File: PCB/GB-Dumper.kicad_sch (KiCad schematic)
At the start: 12 parts, among them J1 GameBoy_Cartridge_MountingPin, J2 Conn_01x03_Male, J3 Conn_01x02_Male, J4 Conn_01x04_Female, U1 74HC595, U2 74HC595

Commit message: -update design to 0.7 (clk 6 rst jumpers)
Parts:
- added C1: 22 µF, Capacitor_THT:CP_Radial_D4.0mm_P2.00mm, symbol Device:C_Polarized_Small
- R1, R2, R3, R4: value 470 -> 470Ω
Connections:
- net GND: now also C1.2
- net at A1.27 (+5V), J3.1 (Pin_1), J4.2 (Pin_2)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: now also C1.1
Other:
- moved on the sheet: R4
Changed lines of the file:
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@@
   (title_block
     (title "Arduino-Nano-GB-Dumper")
-    (date "13.09.2022")
-    (rev "0.6")
+    (date "2023-05-16")
+    (rev "0.7")
     (company "(C) WodoWiesel")
   )
@@
   )
   (junction (at 88.9 74.93) (diameter 0) (color 0 0 0 0)
+  )
+  (junction (at 78.74 48.26) (diameter 0) (color 0 0 0 0)
   )
   (junction (at 76.2 116.84) (diameter 0) (color 0 0 0 0)
@@
     (stroke (width 0) (type default) (color 0 0 0 0))
   )
+  (wire (pts (xy 69.85 48.26) (xy 72.39 48.26))
+    (stroke (width 0) (type default) (color 0 0 0 0))
+  )
   (wire (pts (xy 181.61 53.34) (xy 213.36 53.34))
     (stroke (width 0) (type default) (color 0 0 0 0))
@@
     (stroke (width 0) (type default) (color 0 0 0 0))
   )
-  (wire (pts (xy 78.74 44.45) (xy 78.74 63.5))
+  (wire (pts (xy 78.74 44.45) (xy 78.74 48.26))
     (stroke (width 0) (type default) (color 0 0 0 0))
   )
@@
     (stroke (width 0) (type default) (color 0 0 0 0))
   )
-  (wire (pts (xy 96.52 48.26) (xy 171.45 48.26))
+  (wire (pts (xy 96.52 48.26) (xy 144.78 48.26))
     (stroke (width 0) (type default) (color 0 0 0 0))
   )
@@
     (stroke (width 0) (type default) (color 0 0 0 0))
   )
+  (wire (pts (xy 78.74 48.26) (xy 78.74 63.5))
+    (stroke (width 0) (type default) (color 0 0 0 0))
+  )
   (wire (pts (xy 76.2 115.57) (xy 76.2 116.84))
     (stroke (width 0) (type default) (color 0 0 0 0))
@@
     (stroke (width 0) (type default) (color 0 0 0 0))
   )
-  (wire (pts (xy 179.07 48.26) (xy 213.36 48.26))
+  (wire (pts (xy 152.4 48.26) (xy 213.36 48.26))
     (stroke (width 0) (type default) (color 0 0 0 0))
   )
@@
   )
   (wire (pts (xy 124.46 124.46) (xy 124.46 123.19))
+    (stroke (width 0) (type default) (color 0 0 0 0))
+  )
+  (wire (pts (xy 77.47 48.26) (xy 78.74 48.26))
     (stroke (width 0) (type default) (color 0 0 0 0))
   )
@@
     )
     (property "Datasheet" "~" (id 3) (at 170.18 156.21 0)
+      (effects (font (size 1.27 1.27)) hide)
+    )
+    (pin "1")
+    (pin "2")
+  )
+  (symbol (lib_id "Device:C_Polarized_Small") (at 74.93 48.26 270) (unit 1)
+    (in_bom yes) (on_board yes)
+    (property "Reference" "C1" (id 0) (at 75.4761 41.91 90))
+    (property "Value" "22 µF" (id 1) (at 74.93 44.45 90))
+    (property "Footprint" "Capacitor_THT:CP_Radial_D4.0mm_P2.00mm" (id 2) (at 74.93 48.26 0)
+      (effects (font (size 1.27 1.27)) hide)
+    )
+    (property "Datasheet" "~" (id 3) (at 74.93 48.26 0)
       (effects (font (size 1.27 1.27)) hide)
     )
@@
     (in_bom yes) (on_board yes)
     (property "Reference" "R2" (id 0) (at 166.37 43.18 90))
-    (property "Value" "470" (id 1) (at 166.37 40.64 90))
+    (property "Value" "470Ω" (id 1) (at 166.37 40.64 90))
     (property "Footprint" "Resistor_THT:R_Axial_DIN0204_L3.6mm_D1.6mm_P7.62mm_Horizontal" (id 2) (at 166.37 44.958 90)
       (effects (font (size 1.27 1.27)) hide)
@@
     (pin "1")
     (pin "2")
+  )
+  (symbol (lib_id "power:GND") (at 69.85 48.26 0) (unit 1)
+    (in_bom yes) (on_board yes)
+    (property "Reference" "#PWR0103" (id 0) (at 69.85 54.61 0)
+      (effects (font (size 1.27 1.27)) hide)
+    )
+    (property "Value" "GND" (id 1) (at 64.77 48.26 0))
+    (property "Footprint" "" (id 2) (at 69.85 48.26 0)
+      (effects (font (size 1.27 1.27)) hide)
+    )
+    (property "Datasheet" "" (id 3) (at 69.85 48.26 0)
+      (effects (font (size 1.27 1.27)) hide)
+    )
+    (pin "1")
   )
   (symbol (lib_id "Connector:Conn_01x03_Male") (at 186.69 19.05 180) (unit 1)
@@
     (in_bom yes) (on_board yes)
     (property "Reference" "R1" (id 0) (at 172.72 38.1 90))
-    (property "Value" "470" (id 1) (at 172.72 35.56 90))
+    (property "Value" "470Ω" (id 1) (at 172.72 35.56 90))
     (property "Footprint" "Resistor_THT:R_Axial_DIN0204_L3.6mm_D1.6mm_P7.62mm_Horizontal" (id 2) (at 172.72 39.878 90)
       (effects (font (size 1.27 1.27)) hide)
@@
     (pin "2")
   )
-  (symbol (lib_id "Device:R") (at 175.26 48.26 90) (unit 1)
-    (in_bom yes) (on_board yes)
-    (property "Reference" "R4" (id 0) (at 175.26 48.26 90))
-    (property "Value" "470" (id 1) (at 175.26 45.72 90))
-    (property "Footprint" "Resistor_THT:R_Axial_DIN0204_L3.6mm_D1.6mm_P7.62mm_Horizontal" (id 2) (at 175.26 50.038 90)
-      (effects (font (size 1.27 1.27)) hide)
-    )
-    (property "Datasheet" "~" (id 3) (at 175.26 48.26 0)
+  (symbol (lib_id "Device:R") (at 148.59 48.26 90) (unit 1)
+    (in_bom yes) (on_board yes)
+    (property "Reference" "R4" (id 0) (at 148.59 48.26 90))
+    (property "Value" "470Ω" (id 1) (at 148.59 50.8 90))
+    (property "Footprint" "Resistor_THT:R_Axial_DIN0204_L3.6mm_D1.6mm_P7.62mm_Horizontal" (id 2) (at 148.59 50.038 90)
+      (effects (font (size 1.27 1.27)) hide)
+    )
+    (property "Datasheet" "~" (id 3) (at 148.59 48.26 0)
       (effects (font (size 1.27 1.27)) hide)
     )
@@
     (in_bom yes) (on_board yes)
     (property "Reference" "R3" (id 0) (at 156.21 45.72 90))
-    (property "Value" "470" (id 1) (at 156.21 43.18 90))
+    (property "Value" "470Ω" (id 1) (at 156.21 49.53 90))
     (property "Footprint" "Resistor_THT:R_Axial_DIN0204_L3.6mm_D1.6mm_P7.62mm_Horizontal" (id 2) (at 156.21 47.498 90)
       (effects (font (size 1.27 1.27)) hide)
@@
       (reference "#PWR0102") (unit 1) (value "GND") (footprint "")
     )
+    (path "/c2a6fbf2-d456-4173-b7b4-140a14e2e40e"
+      (reference "#PWR0103") (unit 1) (value "GND") (footprint "")
+    )
     (path "/65a8895e-60d4-4e2b-8fd2-f734af690ffa"
       (reference "A1") (unit 1) (value "Arduino_Nano_v3.x") (footprint "Module:Arduino_Nano")
     )
+    (path "/2bd6b25f-a519-4224-8dd9-2e42d262ce2e"
+      (reference "C1") (unit 1) (value "22 µF") (footprint "Capacitor_THT:CP_Radial_D4.0mm_P2.00mm")
+    )
     (path "/34bb2d5a-a1fd-4187-b623-25a5b805199b"
       (reference "J1") (unit 1) (value "GameBoy_Cartridge_MountingPin") (footprint "Gekkio_Connector_PCBEdge:GameBoy_Cartridge_AGS_1x32-1MP_P1.50mm_Socket_Horizontal")
@@
     )
     (path "/c693858a-1129-4736-ab51-d45f0fe1bbc8"
-      (reference "R1") (unit 1) (value "470") (footprint "Resistor_THT:R_Axial_DIN0204_L3.6mm_D1.6mm_P7.62mm_Horizontal")
+      (reference "R1") (unit 1) (value "470Ω") (footprint "Resistor_THT:R_Axial_DIN0204_L3.6mm_D1.6mm_P7.62mm_Horizontal")
     )
     (path "/6c0814d8-589e-4385-a695-7b08edb63c30"
-      (reference "R2") (unit 1) (value "470") (footprint "Resistor_THT:R_Axial_DIN0204_L3.6mm_D1.6mm_P7.62mm_Horizontal")
+      (reference "R2") (unit 1) (value "470Ω") (footprint "Resistor_THT:R_Axial_DIN0204_L3.6mm_D1.6mm_P7.62mm_Horizontal")
     )
     (path "/e267c532-9ee2-484f-8167-bdfdae44cb51"
-      (reference "R3") (unit 1) (value "470") (footprint "Resistor_THT:R_Axial_DIN0204_L3.6mm_D1.6mm_P7.62mm_Horizontal")
+      (reference "R3") (unit 1) (value "470Ω") (footprint "Resistor_THT:R_Axial_DIN0204_L3.6mm_D1.6mm_P7.62mm_Horizontal")
     )
     (path "/d5224b3b-c216-4c3d-a93d-c943ade0e499"
-      (reference "R4") (unit 1) (value "470") (footprint "Resistor_THT:R_Axial_DIN0204_L3.6mm_D1.6mm_P7.62mm_Horizontal")
+      (reference "R4") (unit 1) (value "470Ω") (footprint "Resistor_THT:R_Axial_DIN0204_L3.6mm_D1.6mm_P7.62mm_Horizontal")
     )
     (path "/161a0297-a52b-49d1-8ab2-281352eaf1e4"

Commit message: -better gnd with mounting holes -cleanup silkscreen -removes orientation crosses -generated new gerbers/exports
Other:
- title: Arduino-Nano-GB-Dumper -> GB-Dumper
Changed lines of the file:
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@@
   (paper "A4")
   (title_block
-    (title "Arduino-Nano-GB-Dumper")
+    (title "GB-Dumper")
     (date "2023-05-16")
     (rev "0.7")

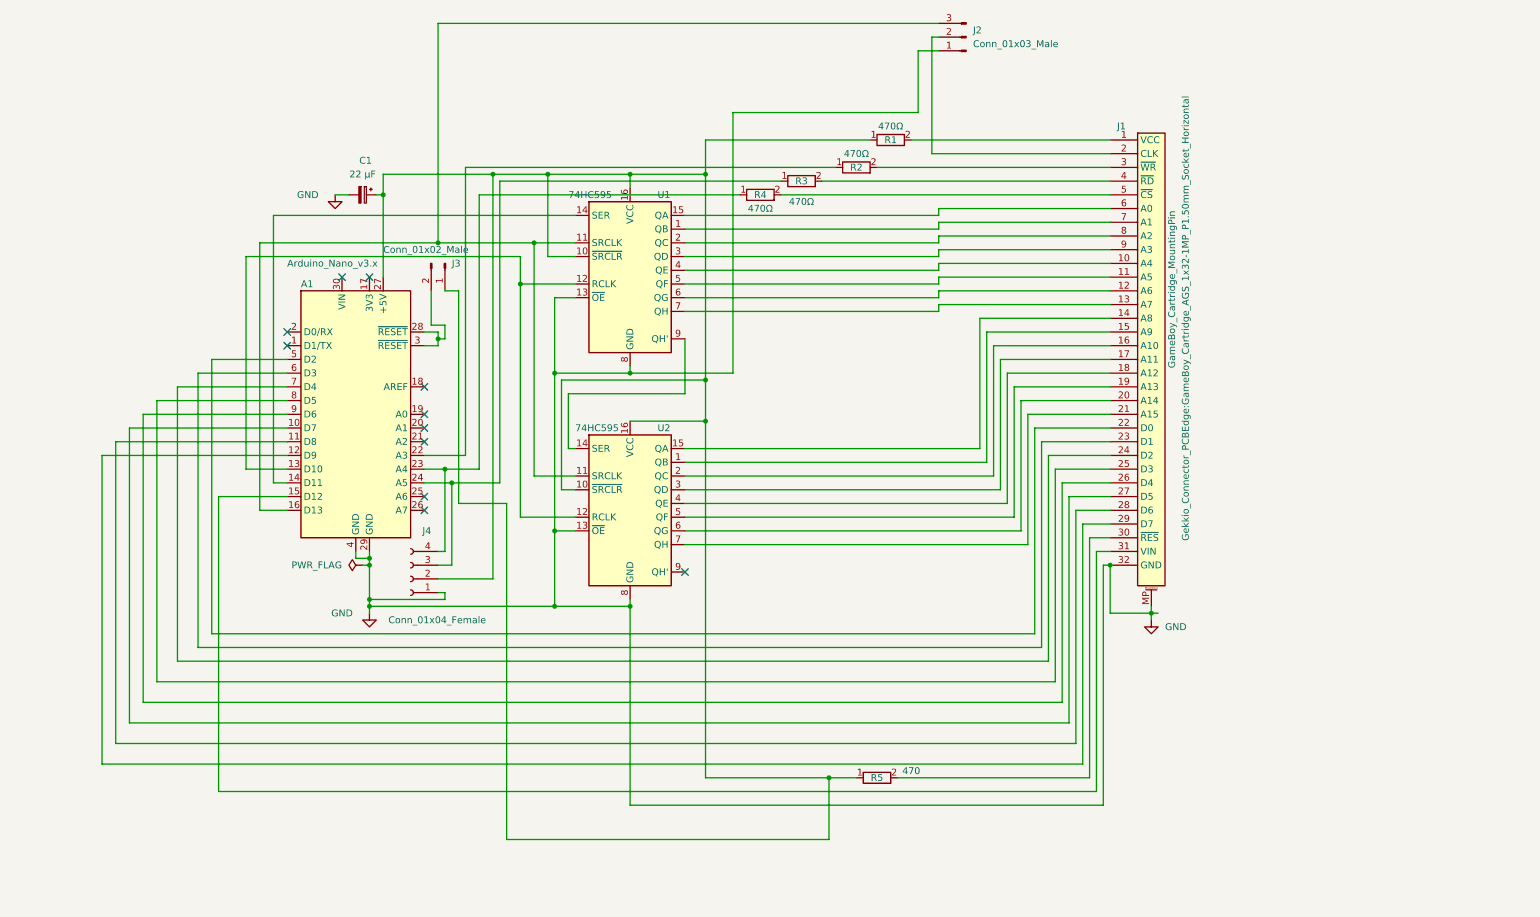
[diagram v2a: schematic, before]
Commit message: better audio + cs2 + rst button support
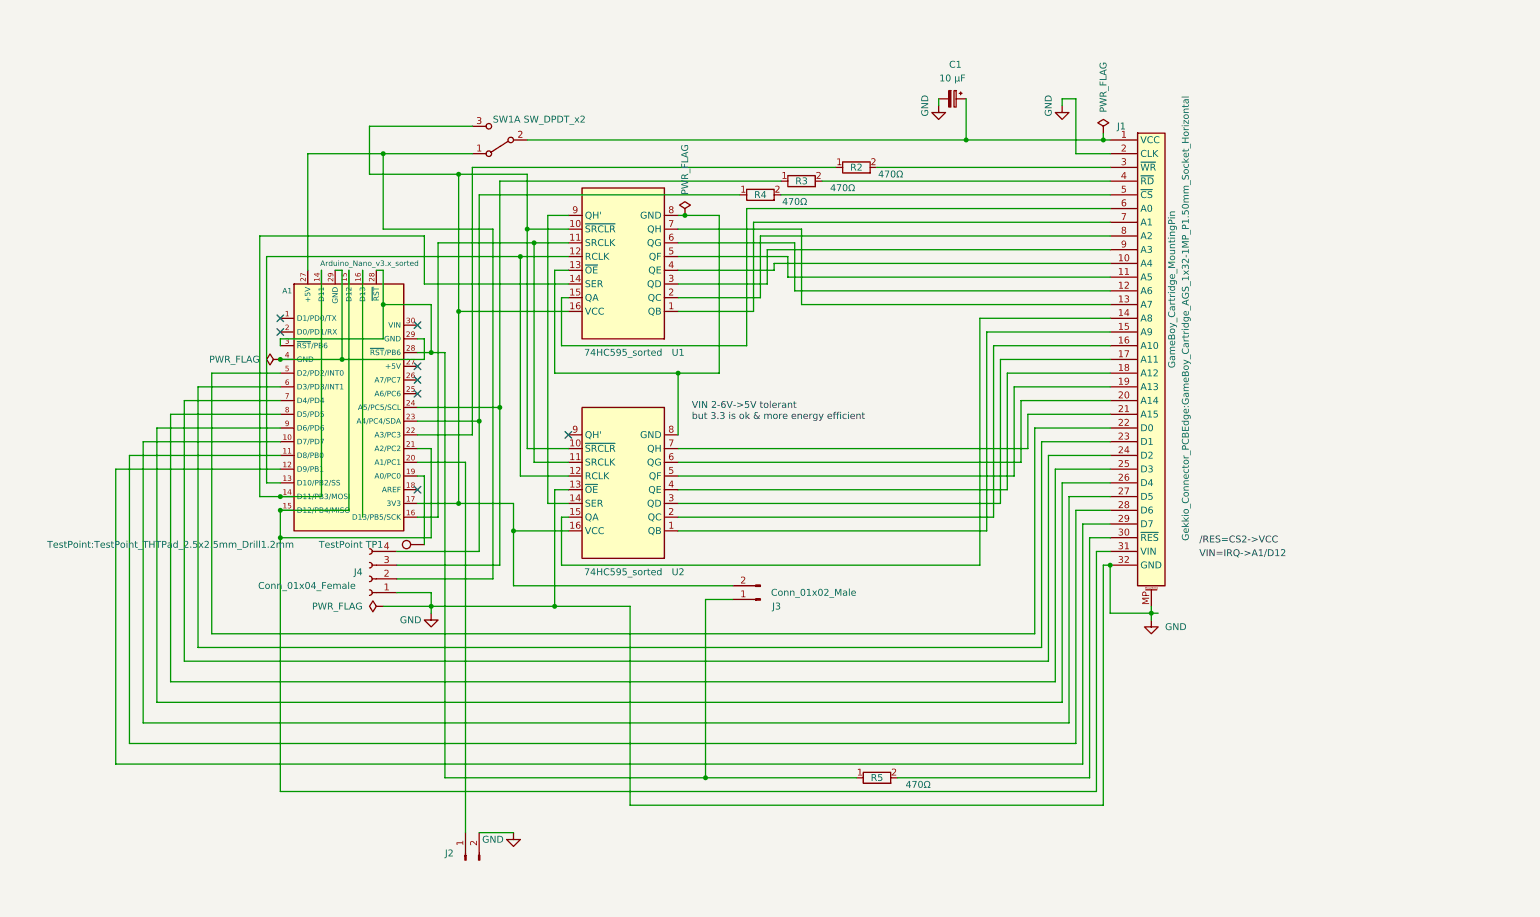
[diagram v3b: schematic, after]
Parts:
- removed A1: Arduino_Nano_v3.x, Module:Arduino_Nano, symbol MCU_Module:Arduino_Nano_v3.x
- removed J2: Conn_01x03_Male, Connector_PinHeader_2.54mm:PinHeader_1x03_P2.54mm_Vertical, symbol Connector:Conn_01x03_Male
- removed R1: 470Ω, Resistor_THT:R_Axial_DIN0204_L3.6mm_D1.6mm_P7.62mm_Horizontal, symbol Device:R
- removed U1, U2: 74HC595, symbol 74xx:74LS595
- added A1: Arduino_Nano_v3.x_sorted, Module:Arduino_Nano, symbol MCU_Module:Arduino_Nano_v3.x_sorted
- added J2: (no value), symbol Connector:Conn_01x02_Male
- added SW1: SW_DPDT_x2, Button_Switch_THT:SW_E-Switch_EG1224_SPDT_Angled, symbol Switch:SW_DPDT_x2
- added TP1: TestPoint, TestPoint:TestPoint_THTPad_2.5x2.5mm_Drill1.2mm, symbol Connector:TestPoint
- added U1, U2: 74HC595_sorted, symbol 74xx:74HC595_sorted
- C1: value 22 µF -> 10 µF
- J4: footprint Connector_PinHeader_2.00mm:PinHeader_1x04_P2.00mm_Vertical -> Connector_PinHeader_2.54mm:PinHeader_1x04_P2.54mm_Vertical
- R5: value 470 -> 470Ω
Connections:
- net GND: now also J1.2 (CLK), J2.2 (Pin_2), U2.13 (~{OE})
- net at J3.1 (Pin_1), R5.1: now also A1.28 (~{RST}/PB6), A1.3 (~{RST}/PB6); no longer C1.1, J4.2 (Pin_2)
- net at J1.1 (VCC): now also C1.1, SW1.2 (B)
- net at J1.10 (A4): now also U1.4 (QE)
- net at J1.11 (A5): now also U1.5 (QF)
- net at J1.12 (A6): now also U1.6 (QG)
- net at J1.13 (A7): now also U1.7 (QH)
- net at J1.14 (A8): now also U2.15 (QA)
- net at J1.15 (A9): now also U2.1 (QB)
- net at J1.16 (A10): now also U2.2 (QC)
- net at J1.17 (A11): now also U2.3 (QD)
- net at J1.18 (A12): now also U2.4 (QE)
- net at J1.19 (A13): now also U2.5 (QF)
- net at J1.20 (A14): now also U2.6 (QG)
- net at J1.21 (A15): now also U2.7 (QH)
- net at J1.22 (D0): now also A1.5 (D2/PD2/INT0)
- net at J1.23 (D1): now also A1.6 (D3/PD3/INT1)
- net at J1.24 (D2): now also A1.7 (D4/PD4)
- net at J1.25 (D3): now also A1.8 (D5/PD5)
- net at J1.26 (D4): now also A1.9 (D6/PD6)
- net at J1.27 (D5): now also A1.10 (D7/PD7)
- net at J1.28 (D6): now also A1.11 (D8/PB0)
- net at J1.29 (D7): now also A1.12 (D9/PB1)
- net at J1.31 (VIN): now also A1.15 (D12/PB4/MISO), A1.21 (A2/PC2)
- net at J1.6 (A0): now also U1.15 (QA)
- net at J1.7 (A1): now also U1.1 (QB)
- net at J1.8 (A2): now also U1.2 (QC)
- net at J1.9 (A3): now also U1.3 (QD)
- net at R2.1: now also A1.22 (A3/PC3)
- net at J4.4 (Pin_4), R4.1: now also A1.23 (A4/PC4/SDA)
- net at J4.3 (Pin_3), R3.1: now also A1.24 (A5/PC5/SCL)
- net at J3.2 (Pin_2): now also A1.17 (3V3), SW1.3 (C), U1.10 (~{SRCLR}), U1.16 (VCC), U2.10 (~{SRCLR}), U2.16 (VCC)
- new net: A1.16 (D13/PB5/SCK), U1.11 (SRCLK), U2.11 (SRCLK)
- new net: A1.13 (D10/PB2/SS), U1.12 (RCLK), U2.12 (RCLK)
- new net: U1.9 (QH'), U2.14 (SER)
- new net: U1.13 (~{OE}), U1.8 (GND), U2.8 (GND)
- new net: A1.19 (A0/PC0), TP1.1
- new net: A1.14 (D11/PB3/MOSI), U1.14 (SER)
- new net: A1.27 (+5V), J4.2 (Pin_2), SW1.1 (A)
- new net: A1.20 (A1/PC1), J2.1 (Pin_1)
- new net: A1.29 (GND), A1.4 (GND)
- no-connect marks 11 -> 8
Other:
- note added: "/RES=CS2->VCC"
- note added: "VIN 2-6V->5V tolerant but 3.3 is ok & more energy efficient"
- note added: "VIN=IRQ->A1/D12"
- moved on the sheet: J4

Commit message: PCB 0.83 update
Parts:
- removed A1: Arduino_Nano_v3.x_sorted, Module:Arduino_Nano, symbol MCU_Module:Arduino_Nano_v3.x_sorted
- removed J2: (no value), symbol Connector:Conn_01x02_Male
- removed J3: Conn_01x02_Male, Connector_PinHeader_2.54mm:PinHeader_1x02_P2.54mm_Vertical, symbol Connector:Conn_01x02_Male
- removed J4: Conn_01x04_Female, Connector_PinHeader_2.54mm:PinHeader_1x04_P2.54mm_Vertical, symbol Connector:Conn_01x04_Female
- removed SW1: SW_DPDT_x2, Button_Switch_THT:SW_E-Switch_EG1224_SPDT_Angled, symbol Switch:SW_DPDT_x2
- added A1: Arduino_Nano_v3.x_sorted, Module:Arduino_Nano_v3.x_sorted, symbol arduino_nano_v3.x_sorted:Arduino_Nano_v3.x_sorted
- added BTN1: SW_Push, Button_Switch_THT:SW_PUSH_6mm, symbol Switch:SW_Push
- added J2, J3, J5: Conn_01x03_Pin, Connector_PinHeader_2.54mm:PinHeader_1x03_P2.54mm_Vertical, symbol Connector:Conn_01x03_Pin
- added J4: Conn_01x04_Pin, Connector_PinHeader_2.54mm:PinHeader_1x04_P2.54mm_Vertical, symbol Connector:Conn_01x04_Pin
- added J7: Conn_01x06_Pin, Connector_PinHeader_2.54mm:PinHeader_1x06_P2.54mm_Vertical, symbol Connector:Conn_01x06_Pin
- added R1: 470Ω, Resistor_THT:R_Axial_DIN0204_L3.6mm_D1.6mm_P7.62mm_Horizontal, symbol Device:R
- added SW1: SW_SPDT, Button_Switch_THT:SW_E-Switch_EG1224_SPDT_Angled, symbol Switch:SW_SPDT
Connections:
- net GND: now also U1.13 (~{OE}), U1.8 (GND), U2.8 (GND), A1.29 (GND), A1.4 (GND), BTN1.2, J4.4 (Pin_4), J5.1 (Pin_1), J7.1 (Pin_1); no longer J1.2 (CLK)
- net at U1.10 (~{SRCLR}), U1.16 (VCC), U2.10 (~{SRCLR})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: now also R5.2, A1.17 (+3V3), J7.6 (Pin_6), R1.2, SW1.3 (C)
- net at U1.11 (SRCLK), U2.11 (SRCLK): now also A1.16 (D13/PB5/SCK), J5.3 (Pin_3), J7.3 (Pin_3)
- net at U1.12 (RCLK), U2.12 (RCLK): now also A1.13 (D10/PB2/SS), J7.5 (Pin_5)
- net at TP1.1: now also A1.19 (A0/PC0)
- net at R5.1: now also J1.30 (~{RES}), J3.2 (Pin_2)
- net at C1.1, J1.1 (VCC): now also SW1.2 (B)
- net at J1.22 (D0): now also A1.2 (D1/PD1/RX)
- net at J1.23 (D1): now also A1.6 (D3/PD3/INT1)
- net at J1.24 (D2): now also A1.7 (D4/PD4)
- net at J1.25 (D3): now also A1.8 (D5/PD5)
- net at J1.26 (D4): now also A1.9 (D6/PD6)
- net at J1.27 (D5): now also A1.10 (D7/PD7)
- net at J1.28 (D6): now also A1.11 (D8/PB0)
- net at J1.29 (D7): now also A1.12 (D9/PB1)
- net at J1.31 (VIN): now also J2.1 (Pin_1)
- net at U1.14 (SER): now also A1.14 (D11/PB3/MOSI), J7.4 (Pin_4)
- net at R2.1: now also A1.22 (A3/PC3)
- net at R4.1: now also A1.23 (A4/PC4/SDA), J4.1 (Pin_1)
- net at R3.1: now also A1.24 (A5/PC5/SCL), J4.2 (Pin_2)
- new net: A1.27 (+5V), J4.3 (Pin_3), SW1.1 (A)
- new net: A1.15 (D12/PB4/MISO), J7.2 (Pin_2)
- new net: J1.2 (CLK), J5.2 (Pin_2)
- new net: A1.1 (D0/PD0/TX), J3.1 (Pin_1)
- new net: A1.28 (~{RST}/PB6), A1.3 (~{RST}/PB6), J3.3 (Pin_3), R1.1
- new net: A1.5 (D2/PD2/INT0), J2.2 (Pin_2)
- new net: A1.21 (A2/PC2), J2.3 (Pin_3)
- new net: A1.20 (A1/PC1), BTN1.1
- no-connect marks 8 -> 11
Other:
- note added: "+3V3"
- note added: "Arduino Clock=16 MHz/4 (SPI-Divider) GB-Clock=4 MHZ"
- note added: "GB ~40mA/5V (max.200mW) GBA ~80mA/3V3 (max.270mW)"
- note added: "GND"
- note added: "I2C(RTC/Disp)"
- note added: "IRQ|GB31|AUD"
- note added: "MISO"
- note added: "MOSI"
- note added: "Micro_SD_Card_SPI"
- note added: "SCK"
- note added: "VCC 2-6V tolerant but 3V3 is ok & more energy efficient"
- note added: "VIN(analog A1-5th sound-ch GB)=IRQ(D12 GBA)"
- note added: "~{CS2}|GB30|~{RST}"
- note added: "~{CS}"
- note added: "~{RES}->VCC(active-low)= ~{CS2}(D0 GBA)"
- note removed: "/RES=CS2->VCC"
- note removed: "VIN 2-6V->5V tolerant but 3.3 is ok & more energy efficient"
- note removed: "VIN=IRQ->A1/D12"
- moved on the sheet: TP1

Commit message: -minor optimizations
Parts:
- removed U1, U2: 74HC595_sorted, symbol 74xx:74HC595_sorted
- added U1, U2: SN74HC595_sorted, Gameboy_THT:SN74HC595, symbol SN74HC595_sorted:74HC595_sorted
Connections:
- net GND: now also U1.13 (~{OE}), U1.8 (GND), U2.16 (VCC), U2.5 (QF)
- net at J1.15 (A9): now also U1.1 (QB)
- net at A1.17 (+3V3), J7.6 (Pin_6), R1.2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: now also U1.10 (~{SRCLR}), U1.16 (VCC), U2.2 (QC), U2.8 (GND)
- net at A1.16 (D13/PB5/SCK), J5.3 (Pin_3), J7.3 (Pin_3): now also U1.11 (SRCLK), U2.3 (QD)
- net at A1.13 (D10/PB2/SS), J7.5 (Pin_5): now also U1.12 (RCLK), U2.4 (QE)
- net at J1.14 (A8): now also U1.15 (QA)
- net at J1.16 (A10): now also U1.2 (QC)
- net at J1.17 (A11): now also U1.3 (QD)
- net at J1.18 (A12): now also U1.4 (QE)
- net at J1.19 (A13): now also U1.5 (QF)
- net at J1.20 (A14): now also U1.6 (QG)
- net at J1.21 (A15): now also U1.7 (QH)
- net at A1.14 (D11/PB3/MOSI), J7.4 (Pin_4): now also U2.6 (QG)
- net at J1.10 (A4): now also U2.12 (RCLK)
- net at J1.11 (A5): now also U2.13 (~{OE})
- net at J1.12 (A6): now also U2.14 (SER)
- net at J1.13 (A7): now also U2.15 (QA)
- net at J1.6 (A0): now also U2.7 (QH)
- net at J1.7 (A1): now also U2.9 (QH')
- net at J1.8 (A2): now also U2.10 (~{SRCLR})
- net at J1.9 (A3): now also U2.11 (SRCLK)
- new net: U1.14 (SER), U2.1 (QB)
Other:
- note added: "Arduino consumption: ~30mA @5V tasks, ~7mA standby total pcb: ~160-250mA tasks, ~10 mA standby"
- note added: "VCC 2-6V tolerant, 5V @67mA & 433ns but 3V3 @44mA & 600ns is more energy efficient"
- note removed: "VCC 2-6V tolerant but 3V3 is ok & more energy efficient"
